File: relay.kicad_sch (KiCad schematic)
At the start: 8 parts, among them J2 Conn_01x02_Pin, K1 SRD-05VDC-SL-C, Q1 S8050, U1 PC817X3NSZ1B

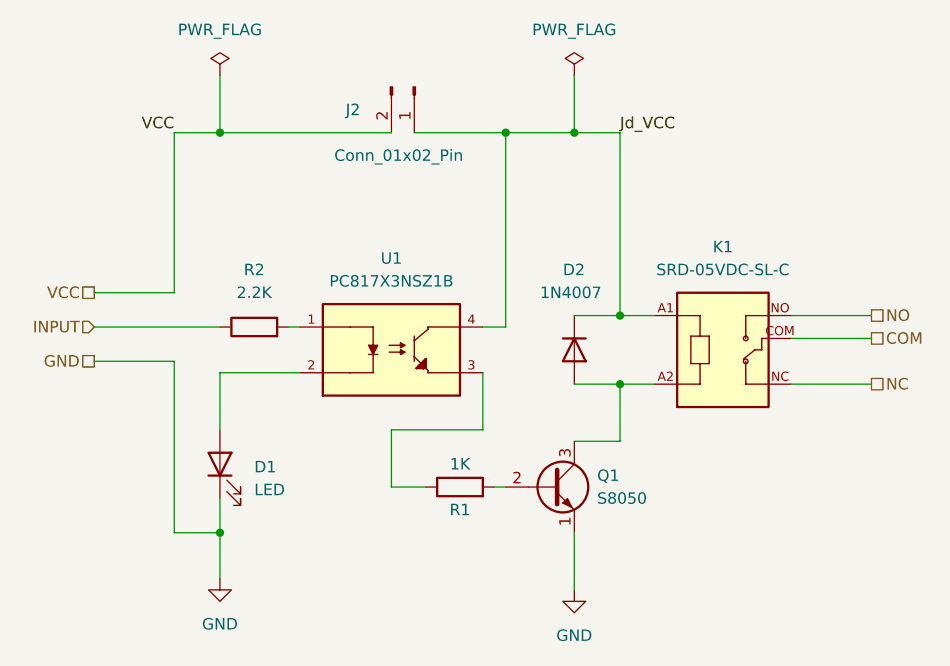
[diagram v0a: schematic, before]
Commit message: Amc1200 Based Voltage Sensing Schematic Completed
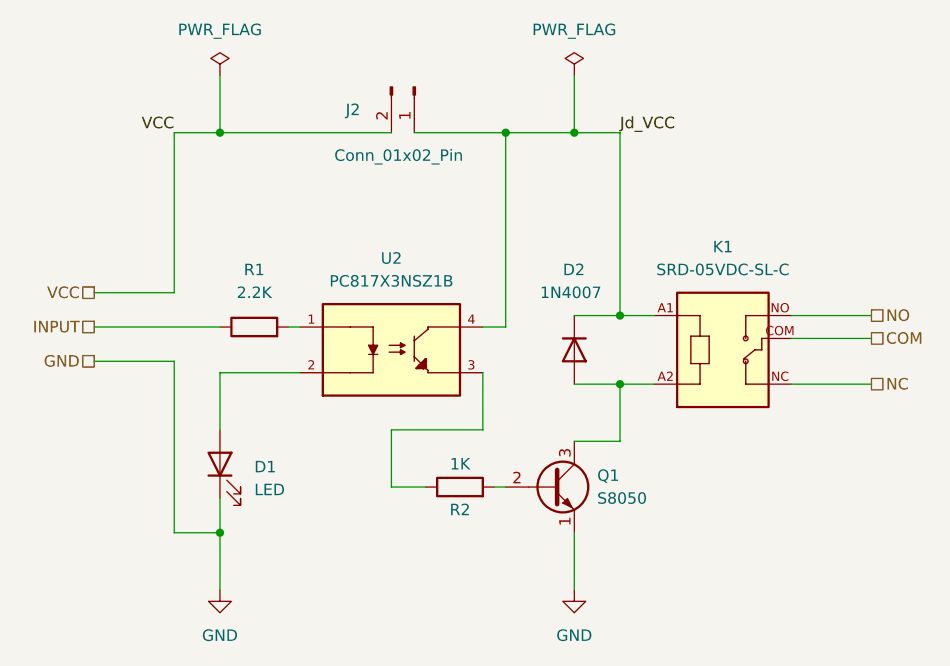
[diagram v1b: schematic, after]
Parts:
- renumbered R2 to R1, R1 to R2, U1 to U2
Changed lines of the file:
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@@
 	(wire
 		(pts
-			(xy 121.92 118.11) (xy 121.92 123.19)
+			(xy 121.92 118.11) (xy 121.92 124.46)
 		)
 		(stroke
@@
 		)
 	)
+	(hierarchical_label "INPUT"
+		(shape passive)
+		(at 107.95 95.25 180)
+		(effects
+			(font
+				(size 1.27 1.27)
+			)
+			(justify right)
+		)
+	)
 	(hierarchical_label "VCC"
 		(shape passive)
@@
 		)
 	)
-	(hierarchical_label "INPUT"
-		(shape input)
-		(at 107.95 95.25 180)
-		(effects
-			(font
-				(size 1.27 1.27)
-			)
-			(justify right)
-		)
-	)
 	(hierarchical_label "GND"
 		(shape passive)
@@
 	(symbol
 		(lib_id "power:GND")
-		(at 121.92 123.19 0)
+		(at 121.92 124.46 0)
 		(unit 1)
 		(exclude_from_sim no)
@@
 		(dnp no)
 		(fields_autoplaced yes)
-		(property "Reference" "#PWR02"
+		(property "Reference" "#PWR01"
+			(at 121.92 130.81 0)
+			(effects
+				(font
+					(size 1.27 1.27)
+				)
+				(hide yes)
+			)
+		)
+		(property "Value" "GND"
 			(at 121.92 129.54 0)
 			(effects
@@
 					(size 1.27 1.27)
 				)
-				(hide yes)
-			)
-		)
-		(property "Value" "GND"
-			(at 121.92 128.27 0)
-			(effects
-				(font
-					(size 1.27 1.27)
-				)
 			)
 		)
 		(property "Footprint" ""
-			(at 121.92 123.19 0)
+			(at 121.92 124.46 0)
 			(effects
 				(font
@@
 		)
 		(property "Datasheet" ""
-			(at 121.92 123.19 0)
+			(at 121.92 124.46 0)
 			(effects
 				(font
@@
 		)
 		(property "Description" "Power symbol creates a global label with name \"GND\" , ground"
-			(at 121.92 123.19 0)
+			(at 121.92 124.46 0)
 			(effects
 				(font
@@
 			(project "ESP_Edgedevice"
 				(path "/8fa9f2a2-260d-4024-b3c1-a0bc52ef0867/c380d0b5-0235-468c-a489-737f32e01687"
-					(reference "#PWR02")
+					(reference "#PWR01")
 					(unit 1)
 				)
@@
 		(on_board yes)
 		(dnp no)
-		(property "Reference" "R1"
+		(property "Reference" "R2"
 			(at 148.59 115.57 90)
 			(effects
@@
 			(project "ESP_Edgedevice"
 				(path "/8fa9f2a2-260d-4024-b3c1-a0bc52ef0867/c380d0b5-0235-468c-a489-737f32e01687"
-					(reference "R1")
+					(reference "R2")
 					(unit 1)
 				)
@@
 		(dnp no)
 		(fields_autoplaced yes)
-		(property "Reference" "R2"
+		(property "Reference" "R1"
 			(at 125.73 88.9 90)
 			(effects
@@
 			(project ""
 				(path "/8fa9f2a2-260d-4024-b3c1-a0bc52ef0867/c380d0b5-0235-468c-a489-737f32e01687"
-					(reference "R2")
+					(reference "R1")
 					(unit 1)
 				)
@@
 		(dnp no)
 		(fields_autoplaced yes)
-		(property "Reference" "#PWR01"
+		(property "Reference" "#PWR02"
 			(at 161.29 130.81 0)
 			(effects
@@
 			(project ""
 				(path "/8fa9f2a2-260d-4024-b3c1-a0bc52ef0867/c380d0b5-0235-468c-a489-737f32e01687"
-					(reference "#PWR01")
+					(reference "#PWR02")
 					(unit 1)
 				)
@@
 		(dnp no)
 		(fields_autoplaced yes)
-		(property "Reference" "U1"
+		(property "Reference" "U2"
 			(at 140.97 87.63 0)
 			(effects
@@
 			(project ""
 				(path "/8fa9f2a2-260d-4024-b3c1-a0bc52ef0867/c380d0b5-0235-468c-a489-737f32e01687"
-					(reference "U1")
+					(reference "U2")
 					(unit 1)
 				)

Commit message: Final Schematic Editing Completed
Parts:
- D1: footprint (none) -> LED_THT:LED_D3.0mm
- R3: renamed from R1; footprint (none) -> Resistor_THT:R_Axial_DIN0207_L6.3mm_D2.5mm_P15.24mm_Horizontal
- R4: renamed from R2; footprint (none) -> Resistor_THT:R_Axial_DIN0207_L6.3mm_D2.5mm_P15.24mm_Horizontal
- renumbered J2 to J5

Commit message: Final Schematic with minor fixes
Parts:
- added R13: 1K, Resistor_THT:R_Axial_DIN0207_L6.3mm_D2.5mm_P15.24mm_Horizontal, symbol Device:R
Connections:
- net GND: now also U2.2, R13.1; no longer D1.1 (K)
- net INPUT: now also D1.2 (A)
- new net: D1.1 (K), R13.2
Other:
- moved on the sheet: D1
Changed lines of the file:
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@@
+	)
+	(junction
+		(at 121.92 118.11)
+		(diameter 0)
+		(color 0 0 0 0)
+	)
+	(junction
+		(at 113.03 95.25)
+		(diameter 0)
+		(color 0 0 0 0)
 	)
 	(junction
@@
 	(wire
 		(pts
+			(xy 113.03 95.25) (xy 113.03 101.6)
+		)
+		(stroke
+			(width 0)
+			(type default)
+		)
+	)
+	(wire
+		(pts
 			(xy 140.97 113.03) (xy 144.78 113.03)
 		)
@@
 	(wire
 		(pts
-			(xy 121.92 106.68) (xy 121.92 100.33)
-		)
-		(stroke
-			(width 0)
-			(type default)
-		)
-	)
-	(wire
-		(pts
-			(xy 121.92 114.3) (xy 121.92 124.46)
-		)
-		(stroke
-			(width 0)
-			(type default)
-		)
-	)
-	(wire
-		(pts
 			(xy 140.97 113.03) (xy 140.97 106.68)
 		)
@@
 	(wire
 		(pts
+			(xy 113.03 109.22) (xy 113.03 110.49)
+		)
+		(stroke
+			(width 0)
+			(type default)
+		)
+	)
+	(wire
+		(pts
 			(xy 152.4 113.03) (xy 153.67 113.03)
 		)
@@
 	(wire
 		(pts
+			(xy 113.03 118.11) (xy 121.92 118.11)
+		)
+		(stroke
+			(width 0)
+			(type default)
+		)
+	)
+	(wire
+		(pts
 			(xy 116.84 73.66) (xy 140.97 73.66)
 		)
@@
 	(wire
 		(pts
-			(xy 107.95 95.25) (xy 121.92 95.25)
+			(xy 107.95 95.25) (xy 113.03 95.25)
+		)
+		(stroke
+			(width 0)
+			(type default)
+		)
+	)
+	(wire
+		(pts
+			(xy 121.92 100.33) (xy 121.92 118.11)
 		)
 		(stroke
@@
 		(pts
 			(xy 143.51 73.66) (xy 153.67 73.66)
+		)
+		(stroke
+			(width 0)
+			(type default)
+		)
+	)
+	(wire
+		(pts
+			(xy 113.03 95.25) (xy 121.92 95.25)
+		)
+		(stroke
+			(width 0)
+			(type default)
+		)
+	)
+	(wire
+		(pts
+			(xy 121.92 118.11) (xy 121.92 124.46)
 		)
 		(stroke
@@
 	(symbol
 		(lib_id "Device:LED")
-		(at 121.92 110.49 90)
+		(at 113.03 105.41 90)
 		(unit 1)
 		(exclude_from_sim no)
@@
 		(fields_autoplaced yes)
 		(property "Reference" "D1"
-			(at 125.73 110.8074 90)
+			(at 116.84 105.7274 90)
 			(effects
 				(font
@@
 		)
 		(property "Value" "LED"
-			(at 125.73 113.3474 90)
+			(at 116.84 108.2674 90)
 			(effects
 				(font
@@
 		)
 		(property "Footprint" "LED_THT:LED_D3.0mm"
-			(at 121.92 110.49 0)
+			(at 113.03 105.41 0)
 			(effects
 				(font
@@
 		)
 		(property "Datasheet" "~"
-			(at 121.92 110.49 0)
+			(at 113.03 105.41 0)
 			(effects
 				(font
@@
 		)
 		(property "Description" "Light emitting diode"
-			(at 121.92 110.49 0)
+			(at 113.03 105.41 0)
 			(effects
 				(font
@@
 		)
 		(property "Sim.Pins" "1=K 2=A"
-			(at 121.92 110.49 0)
+			(at 113.03 105.41 0)
 			(effects
 				(font
@@
 					(unit 1)
 				)
+			)
+		)
+	)
+	(symbol
+		(lib_id "Device:R")
+		(at 113.03 114.3 180)
+		(unit 1)
+		(exclude_from_sim no)
+		(in_bom yes)
+		(on_board yes)
+		(dnp no)
+		(property "Reference" "R13"
+			(at 115.57 114.3 90)
+			(effects
+				(font
+					(size 1.27 1.27)
+				)
+			)
+		)
+		(property "Value" "1K"
+			(at 110.49 114.3 90)
+			(effects
+				(font
+					(size 1.27 1.27)
+				)
+			)
+		)
+		(property "Footprint" "Resistor_THT:R_Axial_DIN0207_L6.3mm_D2.5mm_P15.24mm_Horizontal"
+			(at 114.808 114.3 90)
+			(effects
+				(font
+					(size 1.27 1.27)
+				)
+				(hide yes)
+			)
+		)
+		(property "Datasheet" "~"
+			(at 113.03 114.3 0)
+			(effects
+				(font
+					(size 1.27 1.27)
+				)
+				(hide yes)
+			)
+		)
+		(property "Description" "Resistor"
+			(at 113.03 114.3 0)
+			(effects
+				(font
+					(size 1.27 1.27)
+				)
+				(hide yes)
+			)
+		)
+		(pin "1"
+		)
+		(pin "2"
+		)
+		(instances
+			(project "ESP_Edgedevice"
+				(path "/8fa9f2a2-260d-4024-b3c1-a0bc52ef0867/c380d0b5-0235-468c-a489-737f32e01687"
+					(reference "R13")
+					(unit 1)
+				)
